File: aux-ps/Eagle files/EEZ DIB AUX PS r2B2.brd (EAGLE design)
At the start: 230.5 x 60 mm, 126 parts, among them IC1 MAX31760AEE+, IC2 VIPer35L, IC3 TL431, J1 PF0030/PC, J2 1-726388-2, J3 1-726388-2, J4 1-726388-2, J5 SWEB 8094 AU/GN, Q1 BTA26-600, Q2 BTA26-600, Q3 2N7002, Q4 2N7002, Q5 2N7002, Q6 PSMN0R9-25YLC, SW1 DF62J12S2AHQA, X1 39-28-1063, X2 39-30-1039, X3 ZL231-16KG, X4 47053-1000, X5 47053-1000, X6 22-23-2021

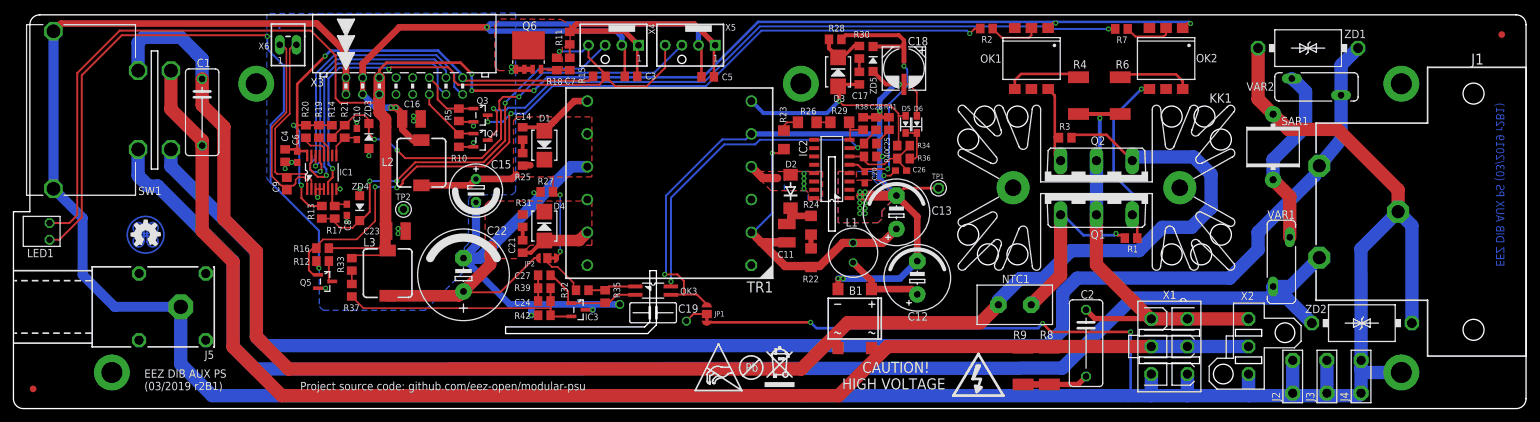
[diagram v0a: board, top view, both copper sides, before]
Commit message: #33, optional 3V3 LDO
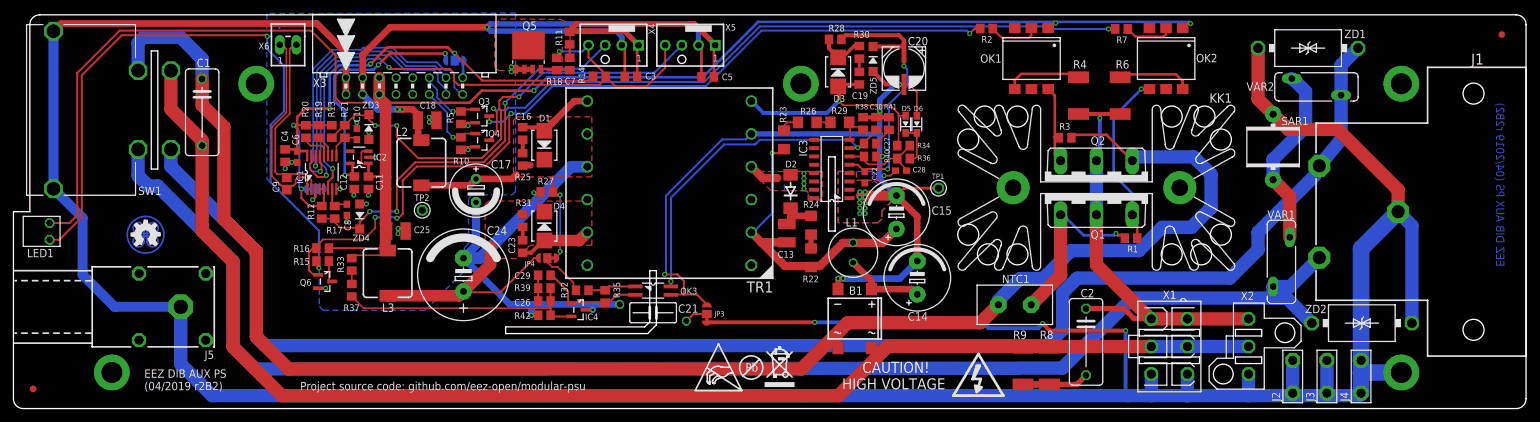
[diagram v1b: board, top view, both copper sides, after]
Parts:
- added C29: 33n, rcl:C0805
- added C30: 2n2, rcl:C0805
- added IC4: TL431, EEZ_Lib1:SOT103P240X110-3N
- added JP3, JP4: JP3-CUT, EEZ_Lib1:JP3-CUT
- C11: value 2n2/1kV -> N.C.; device rcl:C1210 -> rcl:C0805
- C12: value UCY2G6R8MPD -> N.C.; device EEZ_Lib1:ECAP5/10.5 -> rcl:C0805
- C13: value UCY2G6R8MPD -> 2n2/1kV; device EEZ_Lib1:ECAP5/10.5 -> rcl:C1210
- C14: value 3n3 -> UCY2G6R8MPD; device rcl:C0805 -> EEZ_Lib1:ECAP5/10.5
- C15: value UVZ1C471MPD -> UCY2G6R8MPD; device EEZ_Lib1:ECAP3.5/8 -> EEZ_Lib1:ECAP5/10.5
- C16, C23: value 4u7 -> 3n3; device rcl:C1210 -> rcl:C0805
- C17: value 3n3 -> UVZ1C471MPD; device rcl:C0805 -> EEZ_Lib1:ECAP3.5/8
- C18: value EEEFK1V470P -> 4u7; device EEZ_Lib1:CAPAE660X610N -> rcl:C1210
- C19: value CY1Y-470P -> 3n3; device EEZ_Lib1:CY075-032X103 -> rcl:C0805
- C20: value 100n -> EEEFK1V470P; device rcl:C0603 -> EEZ_Lib1:CAPAE660X610N
- C21: value 3n3 -> CY1Y-470P; device rcl:C0805 -> EEZ_Lib1:CY075-032X103
- C22: value 1500u/16V -> 100n; device EEZ_Lib1:ECAP5/13 -> rcl:C0603
- C24: value N.C. -> 1500u/16V; device rcl:C0805 -> EEZ_Lib1:ECAP5/13
- C25: value 33n -> 4u7; device rcl:C0805 -> rcl:C1210
- C26: value 18p -> N.C.; device rcl:C0603 -> rcl:C0805
- C28: value 2n2 -> 18p; device rcl:C0805 -> rcl:C0603
- IC2: value VIPer35L -> (none); device EEZ_Lib1:SOIC-16 -> EEZ_Lib1:SOT95P270X145-5N
- IC3: value TL431 -> VIPer35L; device EEZ_Lib1:SOT103P240X110-3N -> EEZ_Lib1:SOIC-16
- Q5: value 2N7002 -> PSMN0R9-25YLC; device EEZ_Lib1:SOT103P240X110-3N -> EEZ_Lib1:SOT669
- Q6: value PSMN0R9-25YLC -> 2N7002; device EEZ_Lib1:SOT669 -> EEZ_Lib1:SOT103P240X110-3N
- R12: value 470R -> 1K
- R14: value 1K -> 4K7
- R15: value 4K7 -> 470R
- moved C12 87.0 mm to (51.9, 34.4), turned to 270 degrees
- moved C25 73.4 mm to (58.4, 27.1), turned to 0 degrees
- moved C18 73.1 mm to (63.1, 43.9), turned to 0 degrees
- moved IC2 72.0 mm to (52.7, 38.3)
- moved C11 64.2 mm to (54.1, 34.4), turned to 270 degrees
- moved C15 64.2 mm to (134.6, 29.9), turned to 90 degrees
- moved C14 64.0 mm to (137.7, 19.9)
- moved C22 62.9 mm to (129.7, 35.2)
- moved JP1 62.7 mm to (46.0, 33.5), flipped to the bottom, turned to 180 degrees
- moved C17 60.9 mm to (70.5, 33.2)
- moved C26 57.9 mm to (80.9, 16.4), turned to 0 degrees
- moved C27 53.6 mm to (130.6, 40.4)
- moved R15 50.7 mm to (47.1, 22.5)
- moved C19 47.6 mm to (128.9, 50.4), turned to 270 degrees
- moved Q5 46.7 mm to (78.5, 54.4)
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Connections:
- new net N$19: JP2.NC, X3.16
- new net N$23: IC1.3, JP1.COM
- new net N$24: C12.1, IC2.5, JP2.NO
- net +12V: now also C18.1; no longer C16.1
- net +12V_REC: now also C17.+, JP4.NC; no longer C15.+, JP2.NC
- net +3V3: now also IC1.4, IC1.5, JP1.NC, JP2.COM, R12.2, R14.1; no longer R14.2, R15.1, X3.16
- net +5V: now also C11.1, C25.1, IC2.1, IC2.3; no longer C23.1
- net +5V_REC: now also C24.+, JP4.NO; no longer C22.+, JP2.NO
- net 0V: now also C14.-, C15.-, C20.2, C22.1, C30.2, IC3.1, IC3.2, IC3.3, IC3.4, JP3.NO; no longer C12.-, C13.-, C18.2, C20.1, C26.2, IC2.1, IC2.2, IC2.3, IC2.4, JP1.NO
- net 12VAC: now also C16.2; no longer C14.2
- net 5VAC: now also C23.2; no longer C21.2
- net AUX: now also C19.2; no longer C17.2
- net AUX_OUT: now also C20.1, C22.2, IC3.5; no longer C18.1, C20.2, IC2.5
- net DC_BUS: now also C13.1, C15.+; no longer C11.1, C13.+
- net DRAIN: now also Q5.MB; no longer Q6.MB
- net FAN_SENSE1: now also R12.1; no longer R13.1
- net FAN_SENSE2: now also R13.1; no longer R14.1
- net FB1: now also C29.1, IC4.1; no longer C27.1, IC3.1
- net GND: now also C11.2, C12.2, C17.-, C18.2, C21.2, C24.-, C25.2, IC2.2, IC4.3, JP1.NO, Q5.1, Q5.3; no longer C15.-, C16.2, C19.2, C22.-, C23.2, IC1.3, IC1.4, IC1.5, IC3.3, Q6.1, Q6.3
- net N$12: now also JP4.COM; no longer JP2.COM
- net N$13: now also Q6.3, R15.2; no longer Q5.3, R12.2
- net N$137: now also C13.2; no longer C11.2
- net N$138: now also C27.2, C30.1, IC3.7; no longer C25.2, C28.1, IC2.7
- net N$14: now also R15.1; no longer R12.1
- net N$140: now also C19.1; no longer C17.1
- net N$141: now also C28.1, IC3.6; no longer C26.1, IC2.6
- net N$146: now also C23.1; no longer C21.1
- net N$148: now also C26.2, IC4.2; no longer C24.2, IC3.2
- net N$149: now also C26.1, C29.2; no longer C24.1, C27.2
- net N$15: now also Q5.4; no longer Q6.4
- net N$152: now also C27.1; no longer C25.1
- net N$20: now also IC3.8; no longer IC2.8
- net N$4: now also C21.1, JP3.COM; no longer C19.1, JP1.COM
- net N$8: now also C16.1; no longer C14.1
- net N$9: now also C14.+; no longer C12.+
- net PE: now also JP3.NC; no longer JP1.NC
- net PWM_OUT: now also R14.2; no longer R15.2
- net PWR_DIR_OUT: now also Q6.1; no longer Q5.1
- net VIPER_D: now also IC3.13, IC3.14, IC3.15, IC3.16; no longer IC2.13, IC2.14, IC2.15, IC2.16
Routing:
- net N$24: track 0.00 -> 39.1 mm, vias 0 -> 3
- net +3V3: track 87.0 -> 92.7 mm, vias 3 -> 5
- net +5V: track 263.3 -> 267.2 mm, vias 5 -> 3
- net N$23: track 0.00 -> 3.68 mm, vias 0 -> 1
- net N$19: track 0.00 -> 2.63 mm
- net PWM_OUT: track 89.2 -> 91.5 mm
- net SSCL: track 43.4 -> 45.0 mm
- net NFAULT: track 46.5 -> 48.0 mm
- net +12V: track 107.7 -> 109.2 mm
- net PWR_DIRECT: track 9.87 -> 11.2 mm, vias 0 -> 1
- net PWR_SSTART: track 10.3 -> 11.6 mm, vias 0 -> 1
- net PE: track 489.1 -> 487.9 mm
- net SSDA: track 37.7 -> 38.8 mm
- net GND: track 90.9 -> 90.3 mm, vias 20 -> 22
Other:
- board text added: "EEZ DIB AUX PS (04/2019 r2B2)"
- board text removed: "EEZ DIB AUX PS (03/2019 r2B1)"

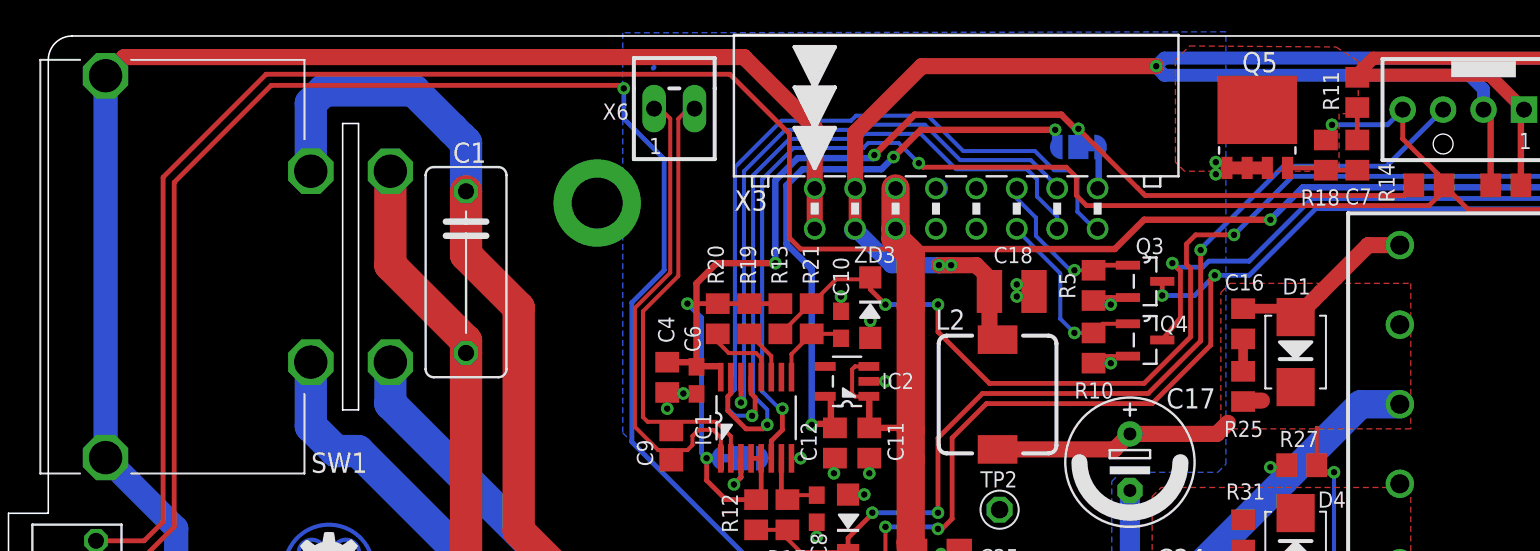
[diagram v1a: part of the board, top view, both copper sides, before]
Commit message: X3 changed to vertical
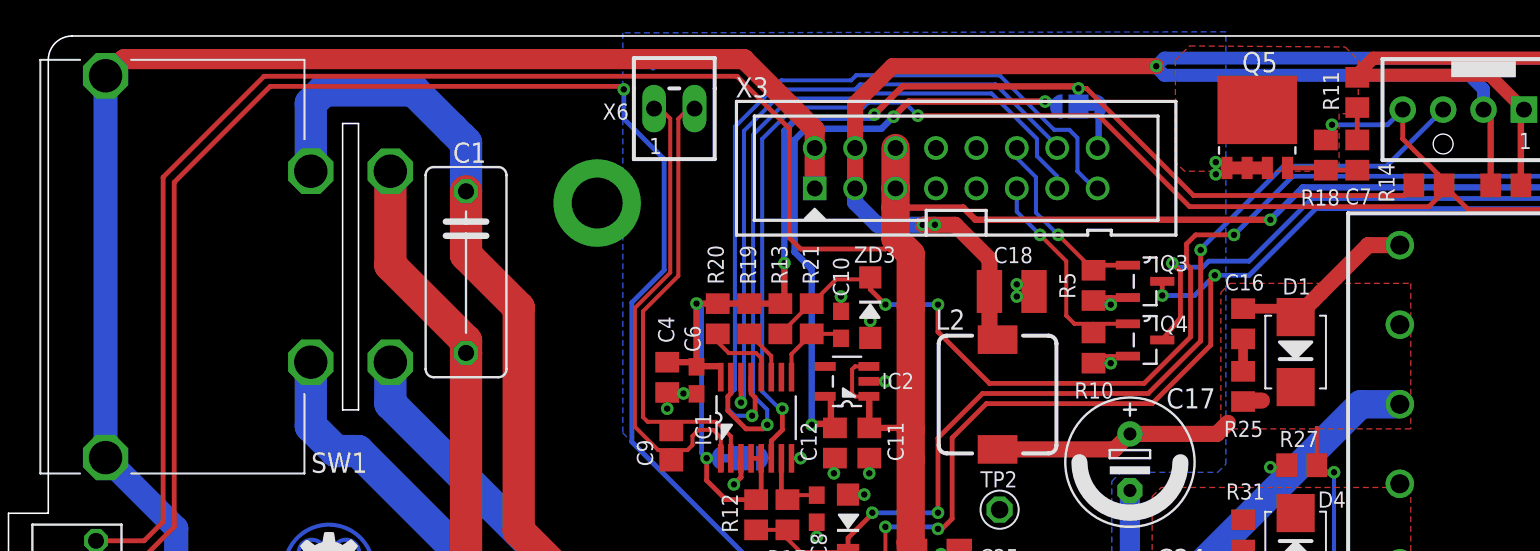
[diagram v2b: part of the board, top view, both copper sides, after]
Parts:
- X3: value ZL231-16KG -> ZL231-16PG; device EEZ_connectors:ML16L -> EEZ_connectors:IDC-16PIN
- moved JP2 2.54 mm to (67.2, 55.6)
- moved X3 2.54 mm to (59.6, 51.7)
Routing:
- net +3V3: track 92.7 -> 89.0 mm
- net +5V: track 267.2 -> 270.2 mm
- net PWM_OUT: track 91.5 -> 94.5 mm
- net PE: track 487.9 -> 485.1 mm
- net SSCL: track 45.0 -> 47.6 mm
- net NFAULT: track 48.0 -> 50.5 mm
- net SSDA: track 38.8 -> 41.4 mm
- net PWR_SSTART: track 11.6 -> 14.0 mm
- net PWR_DIRECT: track 11.2 -> 13.1 mm
- net +12V: track 109.2 -> 110.0 mm
- net N$24: track 39.1 -> 39.9 mm
